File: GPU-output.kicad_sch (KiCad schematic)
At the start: 19 parts

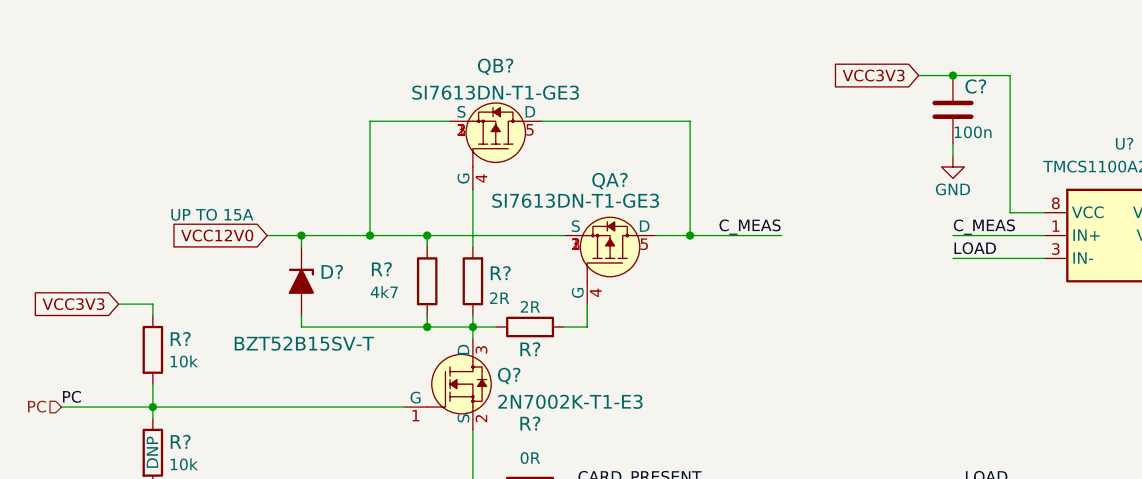
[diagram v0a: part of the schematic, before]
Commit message: Change power flags on schematic
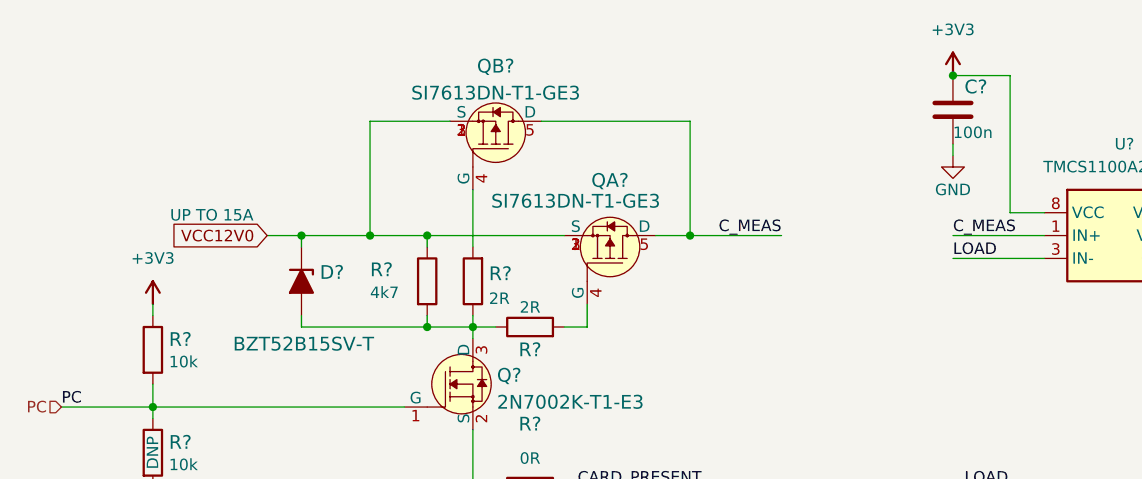
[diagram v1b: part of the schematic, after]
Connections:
- net VCC3V3 renamed +3V3
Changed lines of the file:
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@@
-    (stroke (width 0) (type default) (color 0 0 0 0))
-  )
-  (wire (pts (xy 43.18 60.96) (xy 39.37 60.96))
     (stroke (width 0) (type default) (color 0 0 0 0))
   )
@@
   )
   (wire (pts (xy 73.66 54.61) (xy 73.66 53.34))
-    (stroke (width 0) (type default) (color 0 0 0 0))
-  )
-  (wire (pts (xy 128.27 35.56) (xy 132.08 35.56))
     (stroke (width 0) (type default) (color 0 0 0 0))
   )
@@
     (effects (font (size 1.27 1.27)) (justify left bottom))
   )
-  (global_label "VCC3V3" (shape input) (at 128.27 35.56 180) (fields_autoplaced)
-    (effects (font (size 1.27 1.27)) (justify right))
-    (property "Intersheet References" "${INTERSHEET_REFS}" (id 0) (at 82.55 -36.83 90)
-      (effects (font (size 1.27 1.27)) (justify left) hide)
-    )
-  )
   (global_label "VCC12V0" (shape input) (at 55.88 53.34 180) (fields_autoplaced)
     (effects (font (size 1.27 1.27)) (justify right))
     (property "Intersheet References" "${INTERSHEET_REFS}" (id 0) (at -88.9 -96.52 0)
-      (effects (font (size 1.27 1.27)) hide)
-    )
-  )
-  (global_label "VCC3V3" (shape input) (at 39.37 60.96 180) (fields_autoplaced)
-    (effects (font (size 1.27 1.27)) (justify right))
-    (property "Intersheet References" "${INTERSHEET_REFS}" (id 0) (at -91.44 -92.71 0)
       (effects (font (size 1.27 1.27)) hide)
     )
@@
     (pin "1")
   )
+  (symbol (lib_id "antmicropower:+3V3") (at 132.08 35.56 0) (unit 1)
+    (in_bom yes) (on_board yes) (fields_autoplaced)
+    (property "Reference" "#PWR?" (id 0) (at 147.32 38.1 0)
+      (effects (font (size 1.27 1.27) (thickness 0.15)) (justify left bottom) hide)
+    )
+    (property "Value" "+3V3" (id 1) (at 132.08 30.48 0)
+      (effects (font (size 1.27 1.27) (thickness 0.15)))
+    )
+    (property "Footprint" "" (id 2) (at 147.32 43.18 0)
+      (effects (font (size 1.27 1.27) (thickness 0.15)) (justify left bottom) hide)
+    )
+    (property "Datasheet" "" (id 3) (at 147.32 45.72 0)
+      (effects (font (size 1.27 1.27) (thickness 0.15)) (justify left bottom) hide)
+    )
+    (property "Author" "Antmicro" (id 4) (at 147.32 43.18 0)
+      (effects (font (size 1.27 1.27) (thickness 0.15)) (justify left bottom) hide)
+    )
+    (property "License" "Apache-2.0" (id 5) (at 147.32 45.72 0)
+      (effects (font (size 1.27 1.27) (thickness 0.15)) (justify left bottom) hide)
+    )
+    (pin "1")
+  )
   (symbol (lib_id "antmicroCapacitors0402:C_100n_0402") (at 132.08 39.37 0) (unit 1)
     (in_bom yes) (on_board yes)
@@
     (pin "2")
   )
+  (symbol (lib_id "antmicropower:+3V3") (at 43.18 60.96 0) (unit 1)
+    (in_bom yes) (on_board yes) (fields_autoplaced)
+    (property "Reference" "#PWR?" (id 0) (at 58.42 63.5 0)
+      (effects (font (size 1.27 1.27) (thickness 0.15)) (justify left bottom) hide)
+    )
+    (property "Value" "+3V3" (id 1) (at 43.18 55.88 0)
+      (effects (font (size 1.27 1.27) (thickness 0.15)))
+    )
+    (property "Footprint" "" (id 2) (at 58.42 68.58 0)
+      (effects (font (size 1.27 1.27) (thickness 0.15)) (justify left bottom) hide)
+    )
+    (property "Datasheet" "" (id 3) (at 58.42 71.12 0)
+      (effects (font (size 1.27 1.27) (thickness 0.15)) (justify left bottom) hide)
+    )
+    (property "Author" "Antmicro" (id 4) (at 58.42 68.58 0)
+      (effects (font (size 1.27 1.27) (thickness 0.15)) (justify left bottom) hide)
+    )
+    (property "License" "Apache-2.0" (id 5) (at 58.42 71.12 0)
+      (effects (font (size 1.27 1.27) (thickness 0.15)) (justify left bottom) hide)
+    )
+    (pin "1")
+  )
   (symbol (lib_id "antmicroB2bConnectors:Conn_1-2212115-4") (at 233.68 44.45 0) (unit 1)

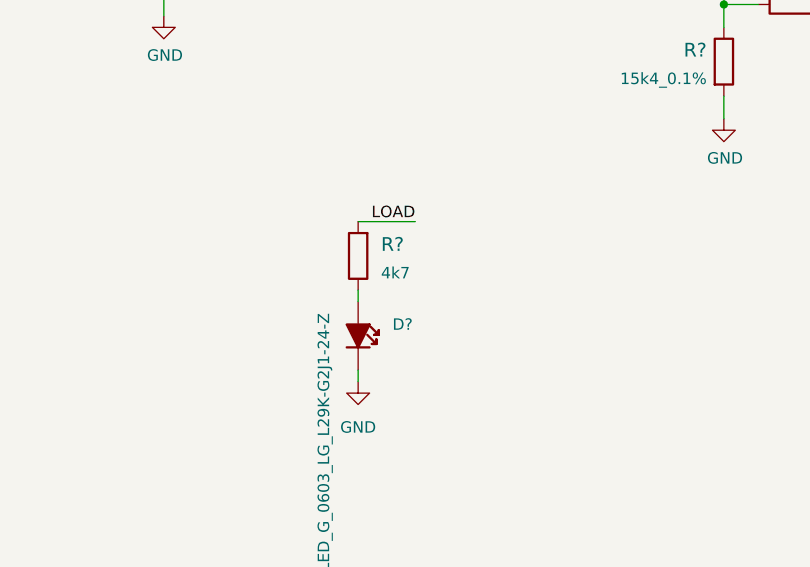
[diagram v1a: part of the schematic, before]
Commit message: Reannotate schematic symbols
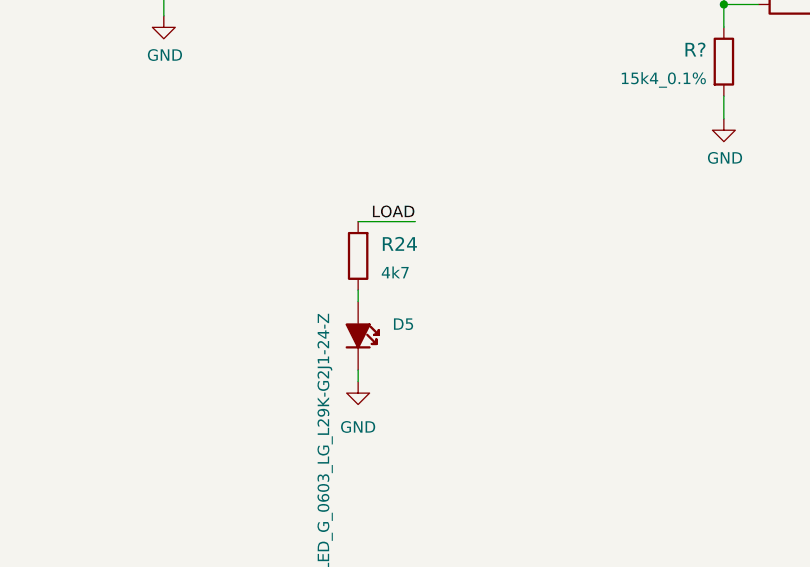
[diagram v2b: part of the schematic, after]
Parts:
- gave numbers to parts that had none: 2
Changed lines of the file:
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@@
   (symbol (lib_id "antmicroResistors0603:R_4k7_0603") (at 100.33 121.92 90) (unit 1)
     (in_bom yes) (on_board yes) (fields_autoplaced)
-    (property "Reference" "R?" (id 0) (at 102.87 120.65 90)
+    (property "Reference" "R24" (id 0) (at 102.87 120.65 90)
       (effects (font (size 1.524 1.524)) (justify right))
     )
@@
   (symbol (lib_id "antmicropower:+3V3") (at 132.08 35.56 0) (unit 1)
     (in_bom yes) (on_board yes) (fields_autoplaced)
-    (property "Reference" "#PWR?" (id 0) (at 147.32 38.1 0)
+    (property "Reference" "#PWR045" (id 0) (at 147.32 38.1 0)
       (effects (font (size 1.27 1.27) (thickness 0.15)) (justify left bottom) hide)
     )
@@
   (symbol (lib_id "antmicropower:+3V3") (at 43.18 60.96 0) (unit 1)
     (in_bom yes) (on_board yes) (fields_autoplaced)
-    (property "Reference" "#PWR?" (id 0) (at 58.42 63.5 0)
+    (property "Reference" "#PWR041" (id 0) (at 58.42 63.5 0)
       (effects (font (size 1.27 1.27) (thickness 0.15)) (justify left bottom) hide)
     )
@@
   (symbol (lib_id "antmicropower:GND") (at 100.33 135.89 0) (unit 1)
     (in_bom yes) (on_board yes) (fields_autoplaced)
-    (property "Reference" "#PWR?" (id 0) (at 100.33 142.24 0)
+    (property "Reference" "#PWR044" (id 0) (at 100.33 142.24 0)
       (effects (font (size 1.27 1.27)) hide)
     )
@@
   (symbol (lib_id "antmicroLEDIndicationDiscrete:LED_G_0603_LG_L29K-G2J1-24-Z") (at 100.33 127 270) (unit 1)
     (in_bom yes) (on_board yes)
-    (property "Reference" "D?" (id 0) (at 104.14 129.5399 90)
+    (property "Reference" "D5" (id 0) (at 104.14 129.5399 90)
       (effects (font (size 1.27 1.27) (thickness 0.15)) (justify left))
     )
